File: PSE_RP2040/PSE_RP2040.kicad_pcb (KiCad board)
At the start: 2 copper layers, 100 x 60 mm, 129 parts, among them IC1 LAN8742A-CZ, IC2 SAM-M8Q-0, J1 USB_B, J2 USB_B_Mini, J3 8P8C_LED, J4 Conn_01x03, J5 Screw_Terminal_01x02, J6 Conn_01x04_Female, Q2 IRLML6402, SW1 SW_Push, SW2 SW_Push, T1 749013011, U1 RP2040, U2 PCF8563T, U4 USBLC6-4SC6, U5 W25Q16JVUSSQ, U6 PAM7Q, U7 TPS2375-1, U8 LMR16006YQ, Y1 Crystal_GND3, Y2 Crystal_GND24, Y3 25MHz

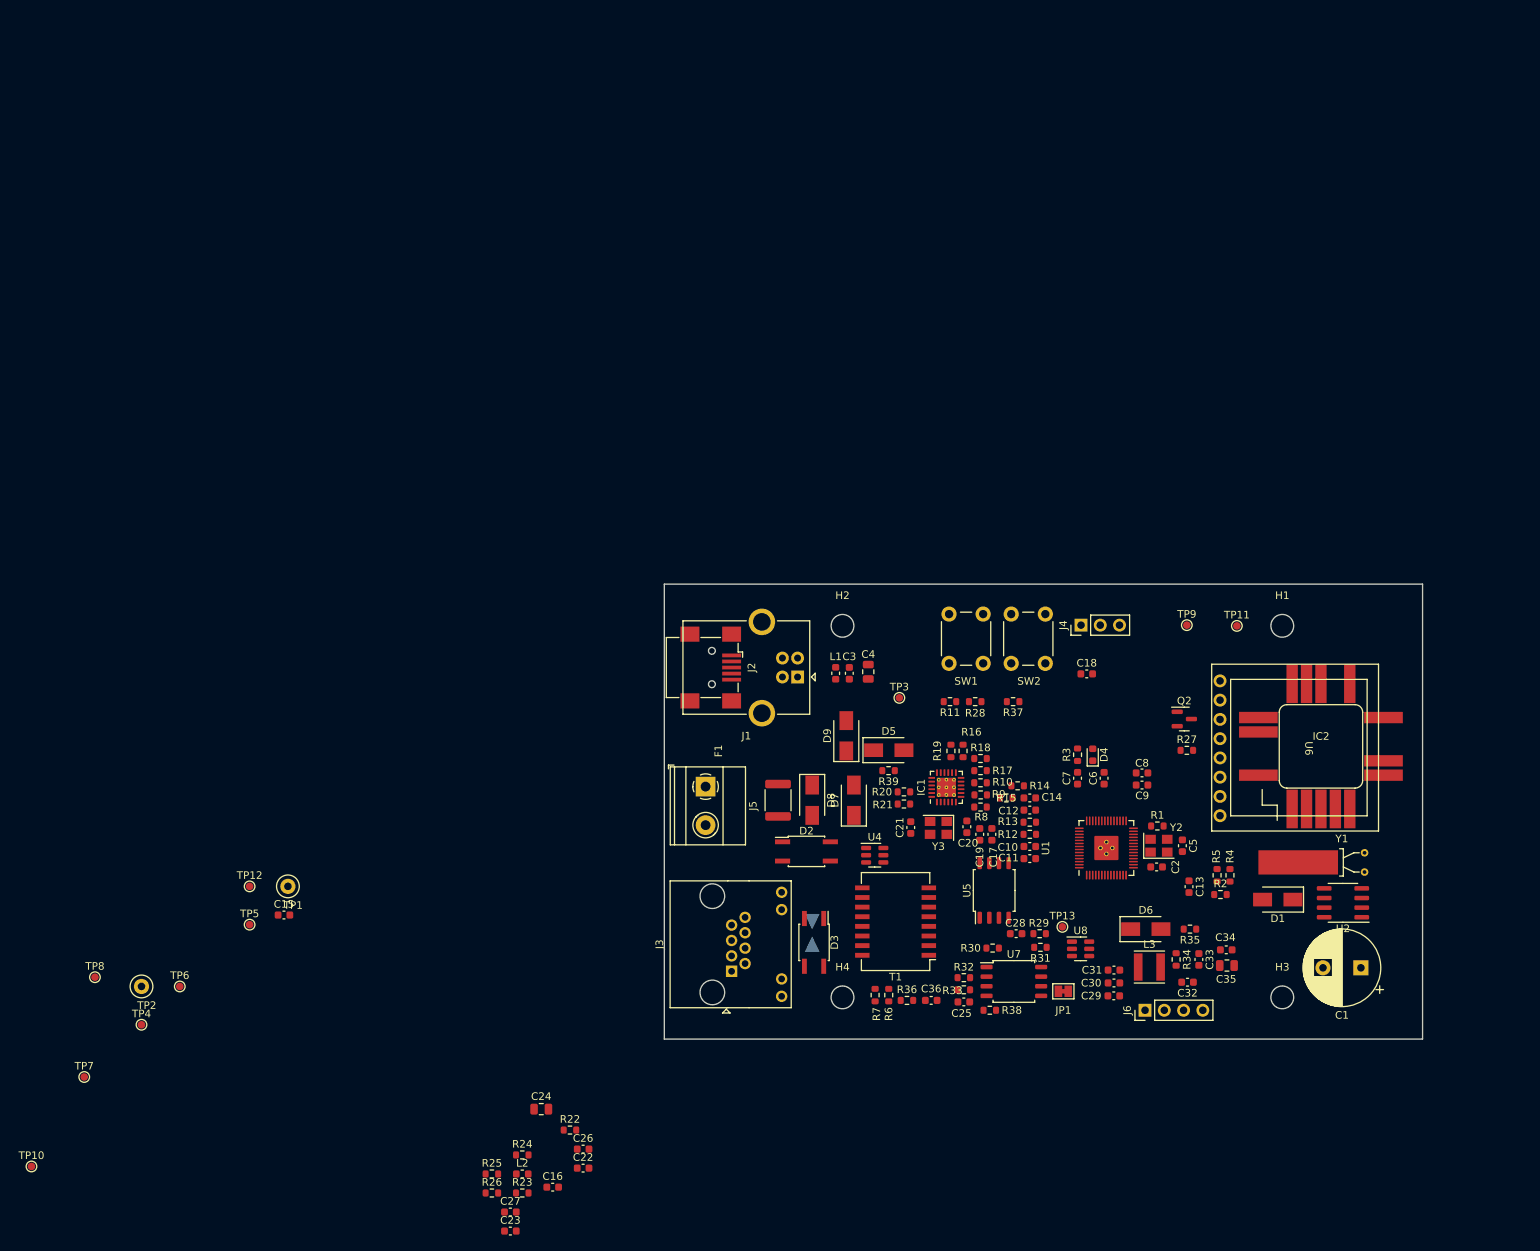
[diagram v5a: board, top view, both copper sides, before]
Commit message: piazzamento componenti pcb
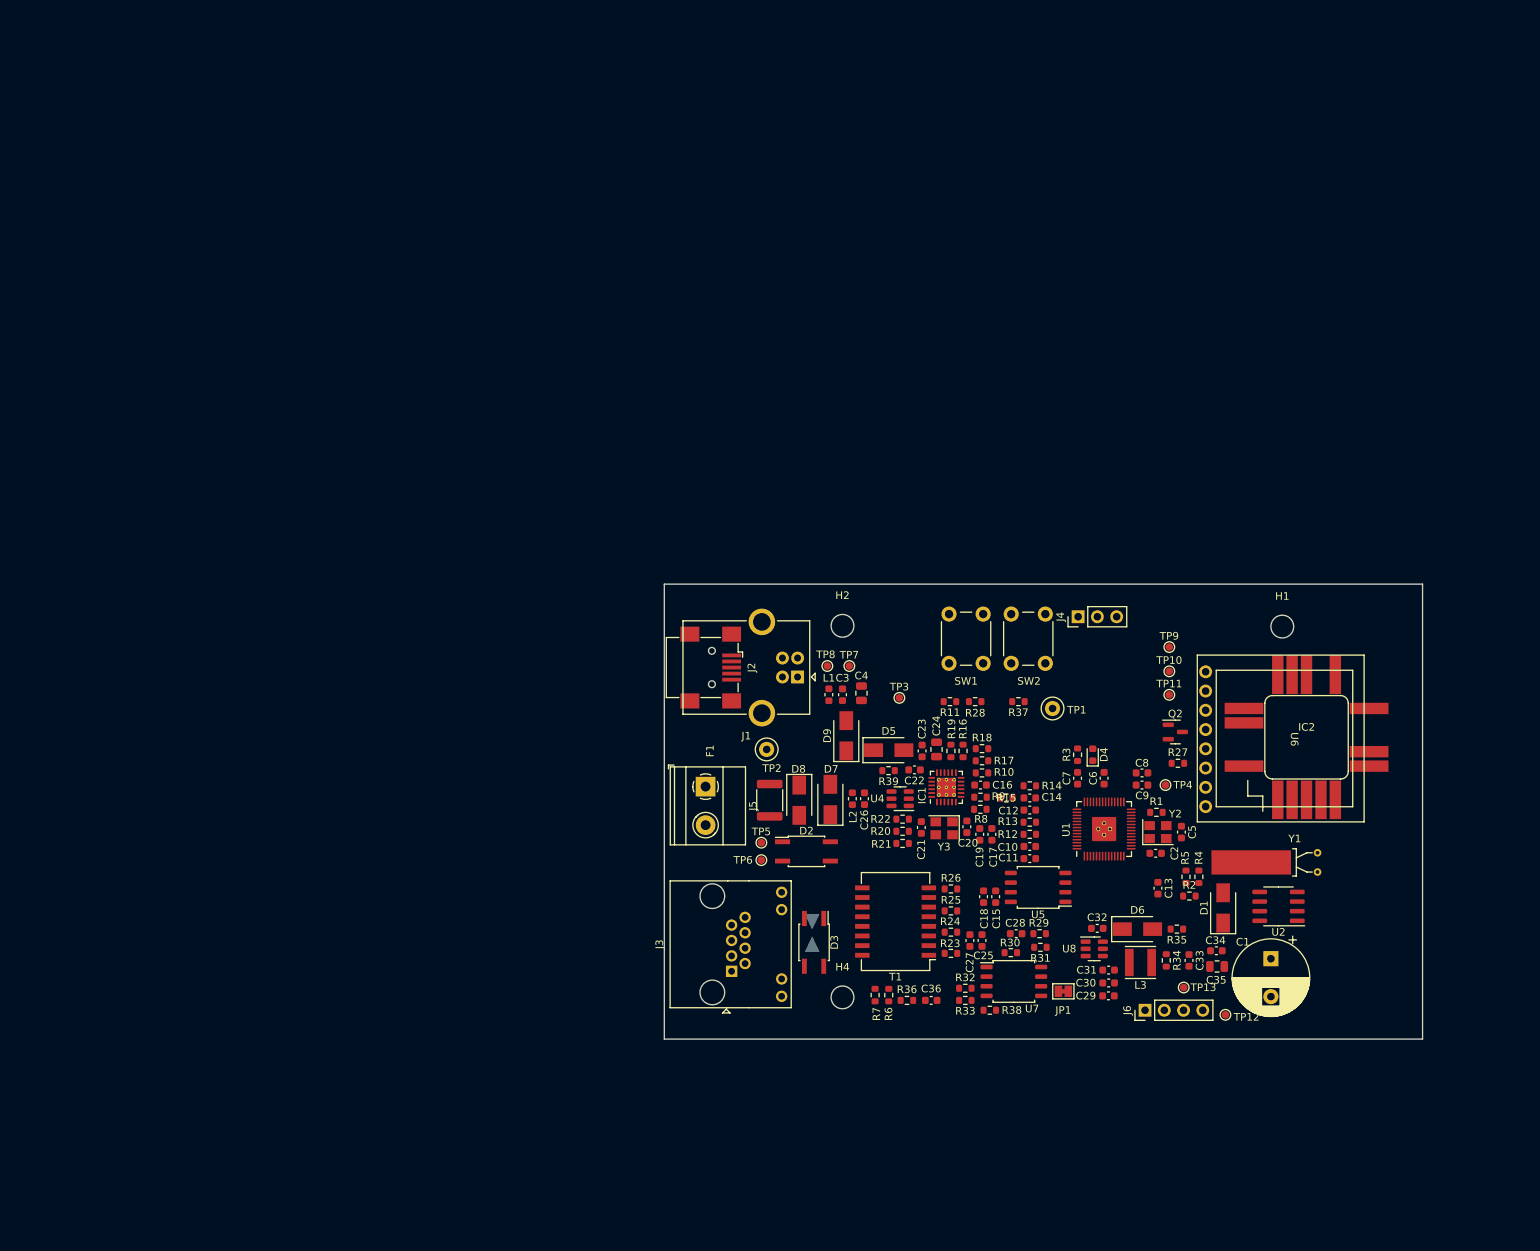
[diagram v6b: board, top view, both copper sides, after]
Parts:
- removed H3: MountingHole, MountingHole:MountingHole_3mm
- moved TP10 163.7 mm to (166.6, 111.5)
- moved TP4 138.7 mm to (166.1, 126.5)
- moved TP12 129.8 mm to (174.0, 156.8)
- moved TP7 114.5 mm to (124.4, 110.8)
- moved TP8 104.9 mm to (121.5, 110.8)
- moved TP1 103.5 mm to (151.2, 116.4)
- moved C15 93.9 mm to (143.7, 141.2), turned to 90 degrees
- moved TP2 88.2 mm to (113.5, 121.8)
- moved C23 83.4 mm to (134.0, 122.0), turned to 90 degrees
- moved TP6 78.5 mm to (112.8, 136.4)
- moved C16 77.4 mm to (141.7, 126.5)
- moved R26 72.6 mm to (137.8, 140.2)
- moved C24 70.5 mm to (135.9, 121.8), turned to 90 degrees
- moved C27 70.4 mm to (140.3, 147.0), turned to 90 degrees
- moved R25 69.8 mm to (137.8, 143.1)
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
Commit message: pcb
spostati componenti
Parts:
- moved H1 49.0 mm to (181.5, 154.6)
- moved Q2 35.4 mm to (166.0, 84.2)
- moved R27 35.4 mm to (166.4, 88.3)
- moved TP10 35.4 mm to (165.2, 76.2)
- moved TP11 35.4 mm to (165.2, 79.3)
- moved TP4 35.4 mm to (164.7, 91.2)
- moved TP9 35.4 mm to (165.2, 73.0)
- moved IC2 12.1 mm to (174.1, 114.4)
- moved U6 11.3 mm to (171.7, 114.5)
- moved J4 8.86 mm to (145.7, 104.4)
- moved SW1 8.86 mm to (128.7, 110.6)
- moved SW2 8.86 mm to (136.9, 110.6)
- moved Y1 8.86 mm to (183.2, 127.1)
- moved U2 8.36 mm to (180.4, 134.2)
- moved D1 8.01 mm to (172.7, 134.7)
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
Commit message: pcb merdaccia
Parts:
- removed C36: 10n, Capacitor_SMD:C_0603_1608Metric
- removed R36: 1M, Resistor_SMD:R_0603_1608Metric
- added H3: MountingHole, MountingHole:MountingHole_3mm, F.Cu at (131.4, 166.2)
- moved TP10 32.0 mm to (156.7, 107.0)
- moved TP11 32.0 mm to (156.7, 110.1)
- moved TP4 32.0 mm to (156.2, 122.0)
- moved TP9 32.0 mm to (156.7, 103.8)
- moved Q2 32.0 mm to (157.5, 115.0)
- moved R27 32.0 mm to (157.9, 119.1)
- moved D2 21.0 mm to (129.2, 153.4), turned to 90 degrees
- moved D3 17.2 mm to (135.9, 153.3), turned to 90 degrees
- moved E1 16.1 mm to (103.4, 146.6)
- moved R7 15.5 mm to (118.1, 142.1), turned to -90 degrees
- moved R6 11.5 mm to (118.1, 155.2)
- moved C25 7.53 mm to (139.5, 139.9), turned to -90 degrees
- moved R23 7.07 mm to (131.3, 145.8), turned to 90 degrees
- moved R26 6.71 mm to (131.3, 138.6), turned to -90 degrees
- moved T1 6.21 mm to (124.7, 142.2)
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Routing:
- net Net-(D2-Pad3): track 0.00 -> 30.0 mm
- net Net-(D2-Pad4): track 0.00 -> 27.7 mm
- net RX_P: track 0.00 -> 21.1 mm
- net Net-(C22-Pad1): track 0.00 -> 19.7 mm
- net RX_N: track 0.00 -> 14.5 mm, vias 0 -> 1
- net TX_P: track 0.00 -> 13.3 mm, vias 0 -> 1
- net TX_N: track 0.00 -> 12.2 mm, vias 0 -> 1
- net /USB_DN: track 0.00 -> 10.1 mm
- net /USB_DP: track 0.00 -> 7.22 mm
- net Net-(IC1-Pad22): track 0.00 -> 3.95 mm
- net Net-(IC1-Pad21): track 0.00 -> 3.90 mm
- net Net-(J3-Pad9): track 0.00 -> 2.64 mm
- net Net-(J3-Pad11): track 0.00 -> 2.61 mm
- net Net-(IC1-Pad23): track 0.00 -> 2.22 mm
- net Net-(IC1-Pad20): track 0.00 -> 2.17 mm
- added copper zone on F.Cu, net GND
